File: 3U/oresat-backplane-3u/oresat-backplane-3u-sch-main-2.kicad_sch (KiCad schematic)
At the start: 12 parts

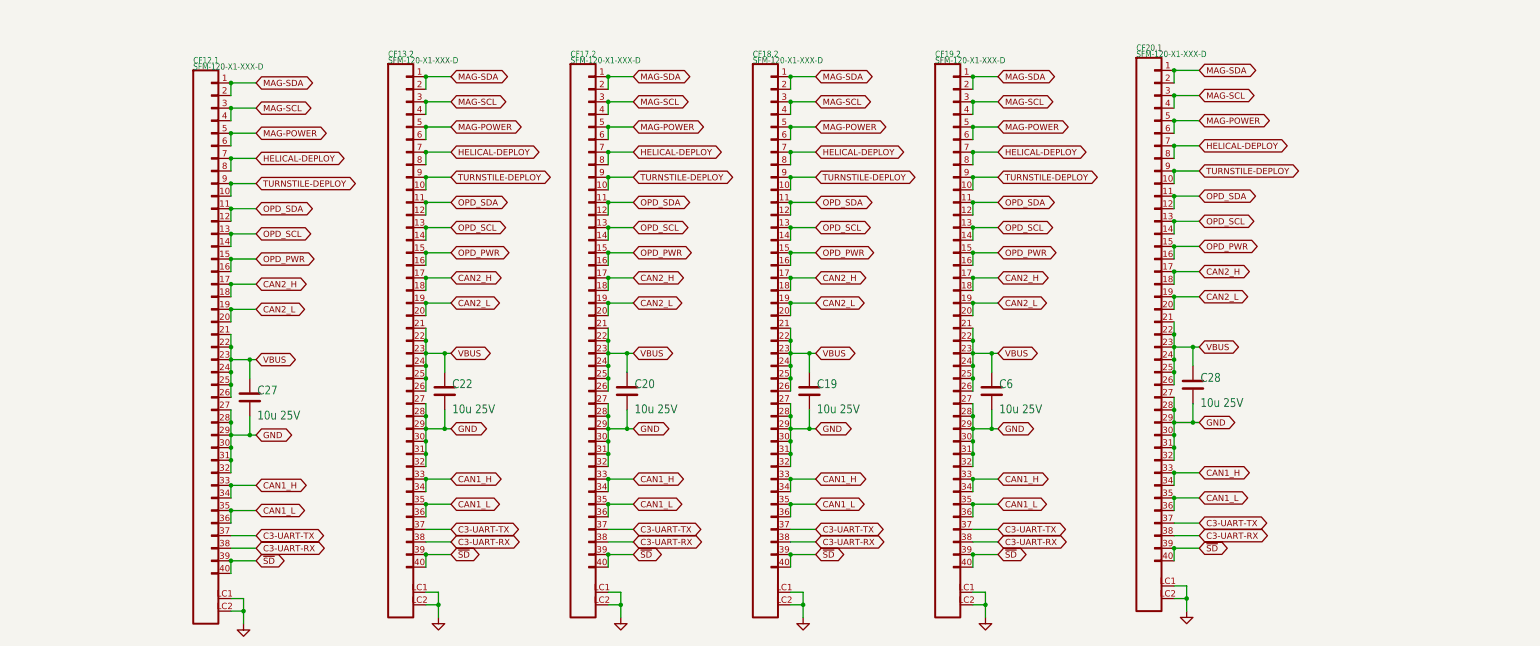
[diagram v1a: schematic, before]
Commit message: Added more Auxiliary connectors
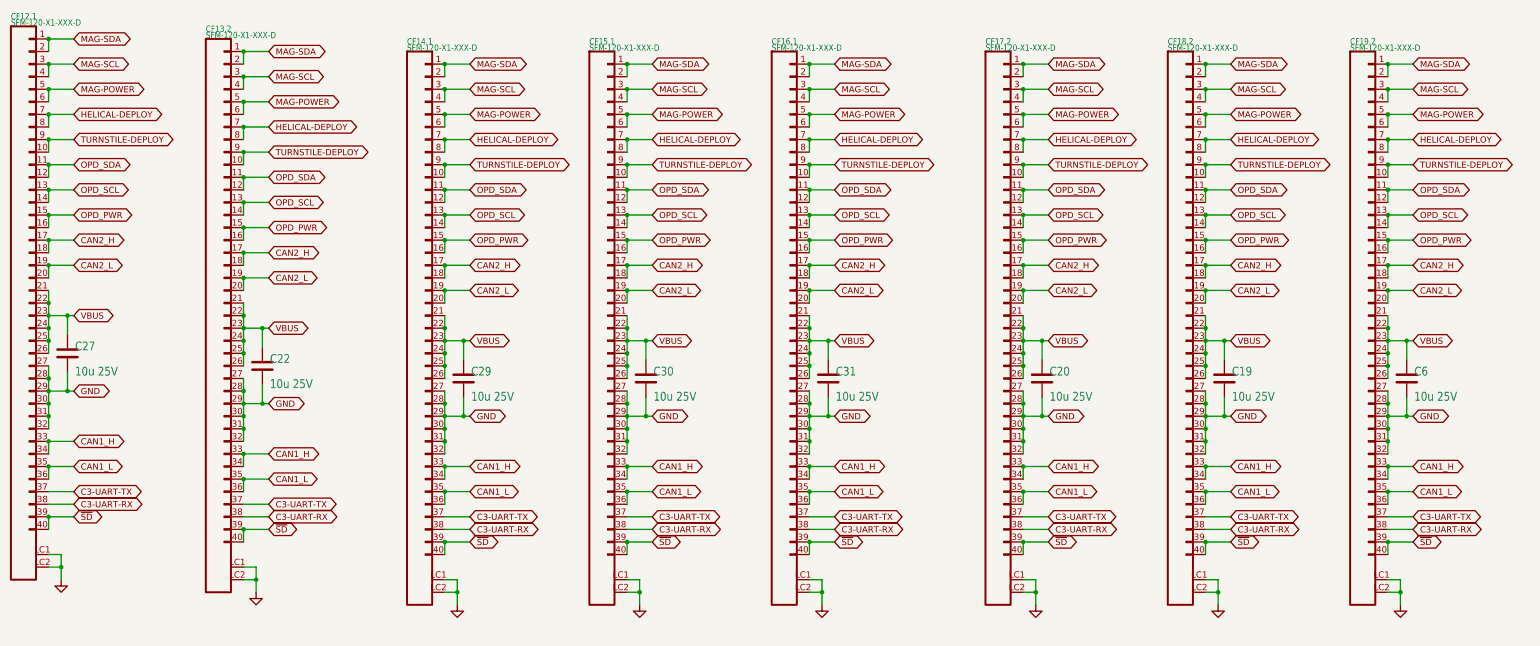
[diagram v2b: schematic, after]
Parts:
- removed C28: 10u 25V, Capacitor_SMD:C_1206_3216Metric, symbol Device:C
- removed CF20.1: SFM-120-X1-XXX-D, oresat-connectors:J-SAMTEC-SFM-120-X1-XXX-D, symbol oresat-connectors:J-SAMTEC-SFM-120-X1-XXX-D
- added C29, C30, C31: 10u 25V, Capacitor_SMD:C_1206_3216Metric, symbol Device:C
- added CF14.1, CF15.1, CF16.1: SFM-120-X1-XXX-D, oresat-connectors:J-SAMTEC-SFM-120-X1-XXX-D, symbol oresat-connectors:J-SAMTEC-SFM-120-X1-XXX-D
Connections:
- net C3-UART-RX: now also CF14.1.38, CF15.1.38, CF16.1.38
- net C3-UART-TX: now also CF14.1.37, CF15.1.37, CF16.1.37
- net CAN1_H: now also CF14.1.33, CF14.1.34, CF15.1.33, CF15.1.34, CF16.1.33, CF16.1.34
- net CAN1_L: now also CF14.1.35, CF14.1.36, CF15.1.35, CF15.1.36, CF16.1.35, CF16.1.36
- net CAN2_H: now also CF14.1.17, CF14.1.18, CF15.1.17, CF15.1.18, CF16.1.17, CF16.1.18
- net CAN2_L: now also CF14.1.19, CF14.1.20, CF15.1.19, CF15.1.20, CF16.1.19, CF16.1.20
- net GND: now also C29.2, C30.2, C31.2, CF14.1.27, CF14.1.28, CF14.1.29, CF14.1.30, CF14.1.31, CF14.1.32, CF14.1.LC1, CF14.1.LC2, CF15.1.27, CF15.1.28, CF15.1.29, CF15.1.30, CF15.1.31, CF15.1.32, CF15.1.LC1, CF15.1.LC2, CF16.1.27, CF16.1.28, CF16.1.29, CF16.1.30, CF16.1.31, CF16.1.32, CF16.1.LC1, CF16.1.LC2
- net HELICAL-DEPLOY: now also CF14.1.7, CF14.1.8, CF15.1.7, CF15.1.8, CF16.1.7, CF16.1.8
- net MAG-POWER: now also CF14.1.5, CF14.1.6, CF15.1.5, CF15.1.6, CF16.1.5, CF16.1.6
- net MAG-SCL: now also CF14.1.3, CF14.1.4, CF15.1.3, CF15.1.4, CF16.1.3, CF16.1.4
- net MAG-SDA: now also CF14.1.1, CF14.1.2, CF15.1.1, CF15.1.2, CF16.1.1, CF16.1.2
- net OPD_PWR: now also CF14.1.15, CF14.1.16, CF15.1.15, CF15.1.16, CF16.1.15, CF16.1.16
- net OPD_SCL: now also CF14.1.13, CF14.1.14, CF15.1.13, CF15.1.14, CF16.1.13, CF16.1.14
- net OPD_SDA: now also CF14.1.11, CF14.1.12, CF15.1.11, CF15.1.12, CF16.1.11, CF16.1.12
- net TURNSTILE-DEPLOY: now also CF14.1.10, CF14.1.9, CF15.1.10, CF15.1.9, CF16.1.10, CF16.1.9
- net VBUS: now also C29.1, C30.1, C31.1, CF14.1.21, CF14.1.22, CF14.1.23, CF14.1.24, CF14.1.25, CF14.1.26, CF15.1.21, CF15.1.22, CF15.1.23, CF15.1.24, CF15.1.25, CF15.1.26, CF16.1.21, CF16.1.22, CF16.1.23, CF16.1.24, CF16.1.25, CF16.1.26
- net ~{SD}: now also CF14.1.39, CF14.1.40, CF15.1.39, CF15.1.40, CF16.1.39, CF16.1.40
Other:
- moved on the sheet: C19, C20, C22, C27, C6, CF12.1, CF13.2, CF17.2, CF18.2, CF19.2

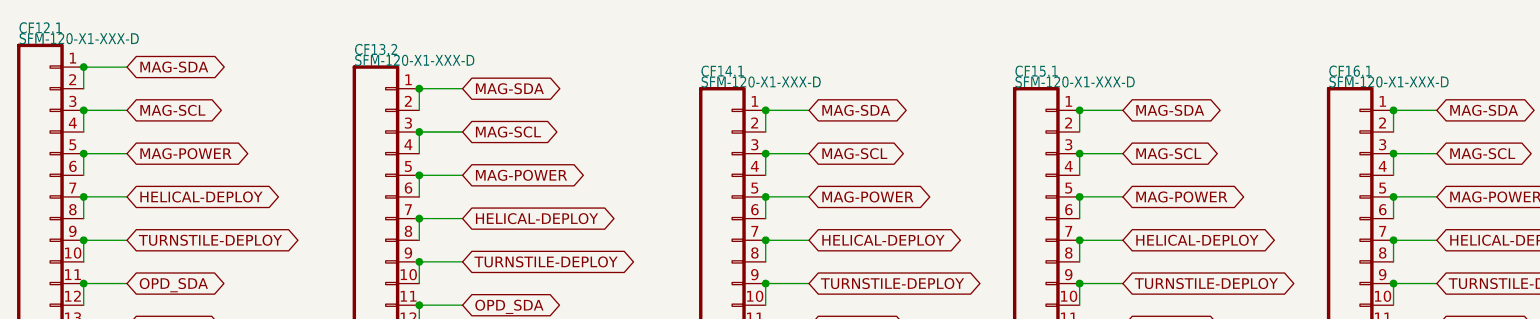
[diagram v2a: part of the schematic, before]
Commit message: Connectors laid out, unrouted
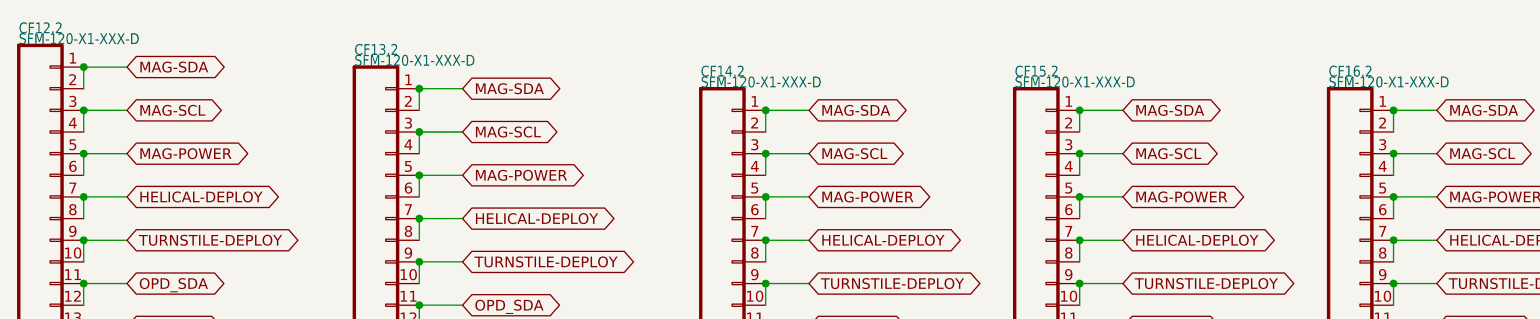
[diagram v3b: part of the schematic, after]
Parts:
- renumbered CF12.1 to CF12.2, CF14.1 to CF14.2, CF15.1 to CF15.2, CF16.1 to CF16.2
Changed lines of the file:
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@@
 		(on_board yes)
 		(dnp no)
-		(property "Reference" "CF12.1"
+		(property "Reference" "CF12.2"
 			(at 76.2 69.85 0)
 			(effects
@@
 			(project "oresat-backplane-3u"
 				(path "/300eeac4-6caf-4310-939c-5dc51539800c/af24dd58-d27a-41e4-b932-04912035cb7a"
-					(reference "CF12.1")
+					(reference "CF12.2")
 					(unit 1)
 				)
@@
 		(on_board yes)
 		(dnp no)
-		(property "Reference" "CF16.1"
+		(property "Reference" "CF16.2"
 			(at 229.87 74.93 0)
 			(effects
@@
 			(project "oresat-backplane-3u"
 				(path "/300eeac4-6caf-4310-939c-5dc51539800c/af24dd58-d27a-41e4-b932-04912035cb7a"
-					(reference "CF16.1")
+					(reference "CF16.2")
 					(unit 1)
 				)
@@
 		(on_board yes)
 		(dnp no)
-		(property "Reference" "CF14.1"
+		(property "Reference" "CF14.2"
 			(at 156.21 74.93 0)
 			(effects
@@
 			(project "oresat-backplane-3u"
 				(path "/300eeac4-6caf-4310-939c-5dc51539800c/af24dd58-d27a-41e4-b932-04912035cb7a"
-					(reference "CF14.1")
+					(reference "CF14.2")
 					(unit 1)
 				)
@@
 		(on_board yes)
 		(dnp no)
-		(property "Reference" "CF15.1"
+		(property "Reference" "CF15.2"
 			(at 193.04 74.93 0)
 			(effects
@@
 			(project "oresat-backplane-3u"
 				(path "/300eeac4-6caf-4310-939c-5dc51539800c/af24dd58-d27a-41e4-b932-04912035cb7a"
-					(reference "CF15.1")
+					(reference "CF15.2")
 					(unit 1)
 				)

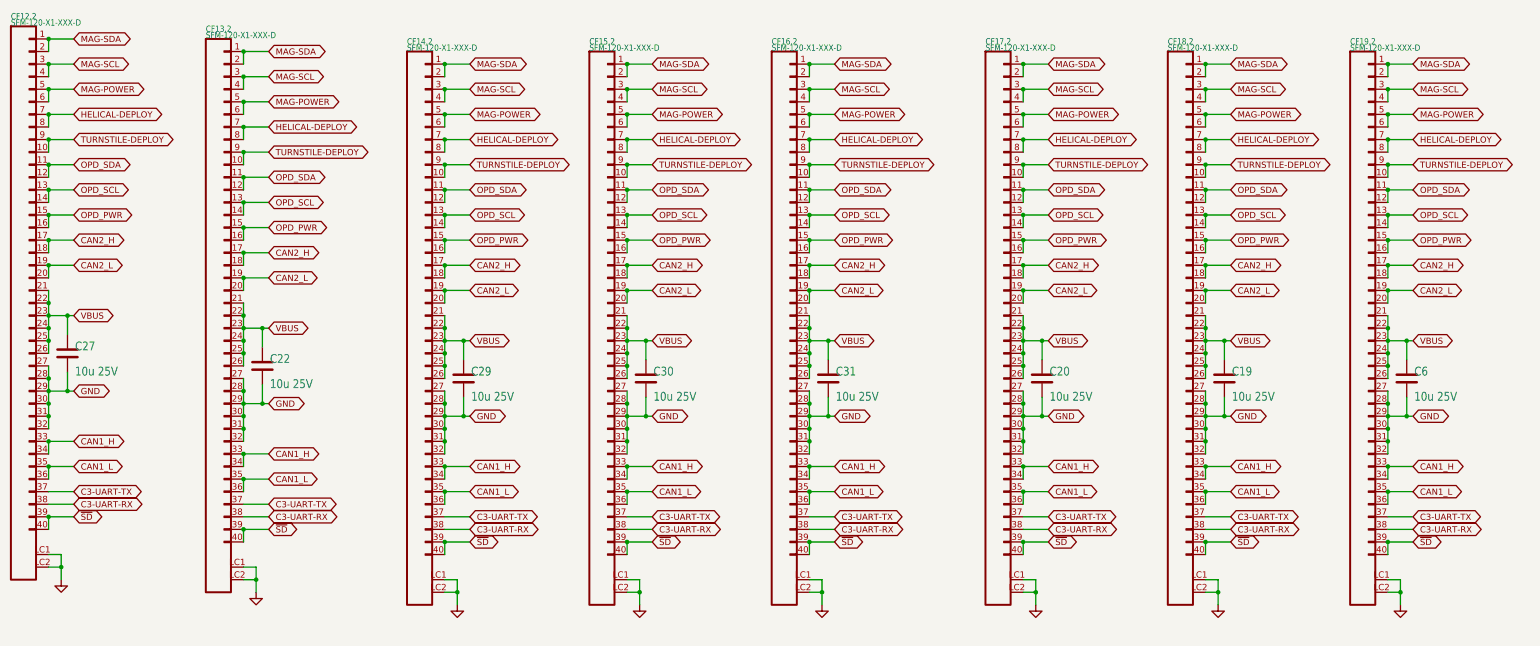
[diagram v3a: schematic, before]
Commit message: Can lines on back - need to move can resistors to front & add b.side solder mask
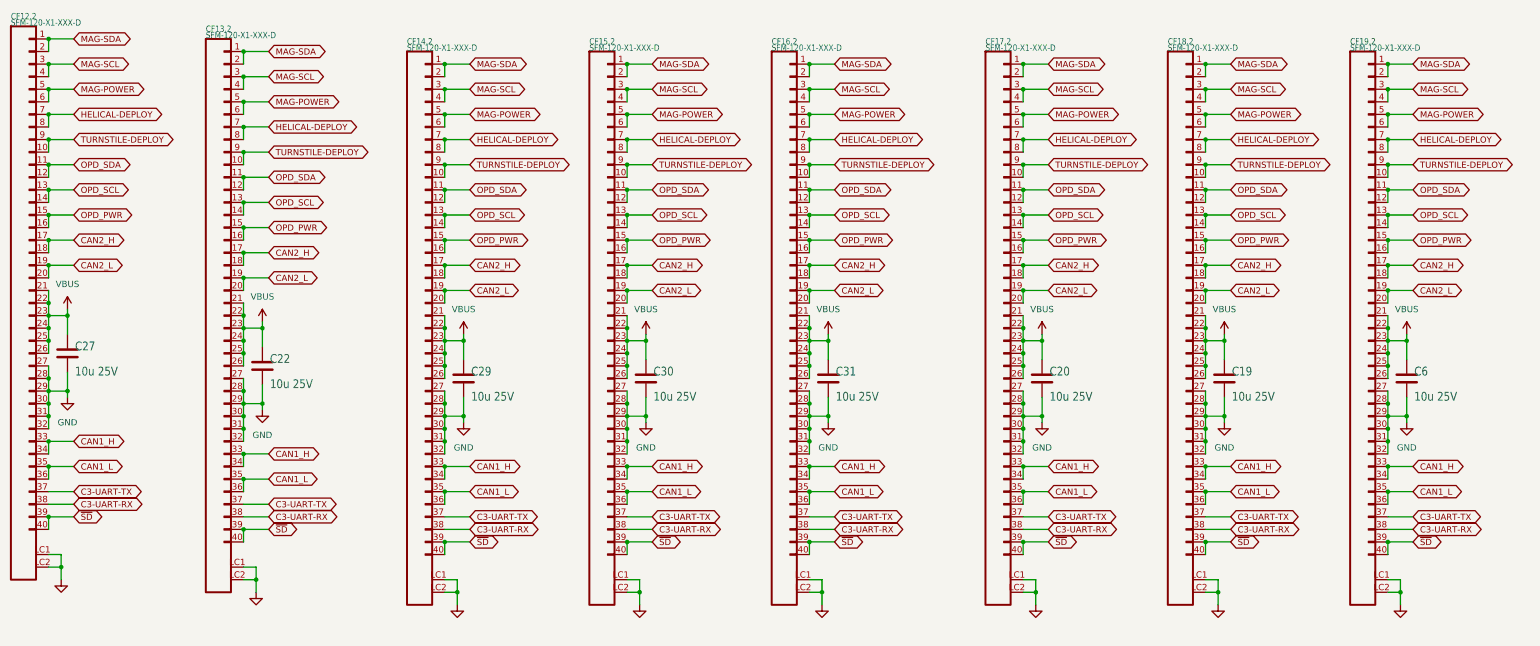
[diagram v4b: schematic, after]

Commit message: Back solder mask added & can resistors moved to F.cu. Final
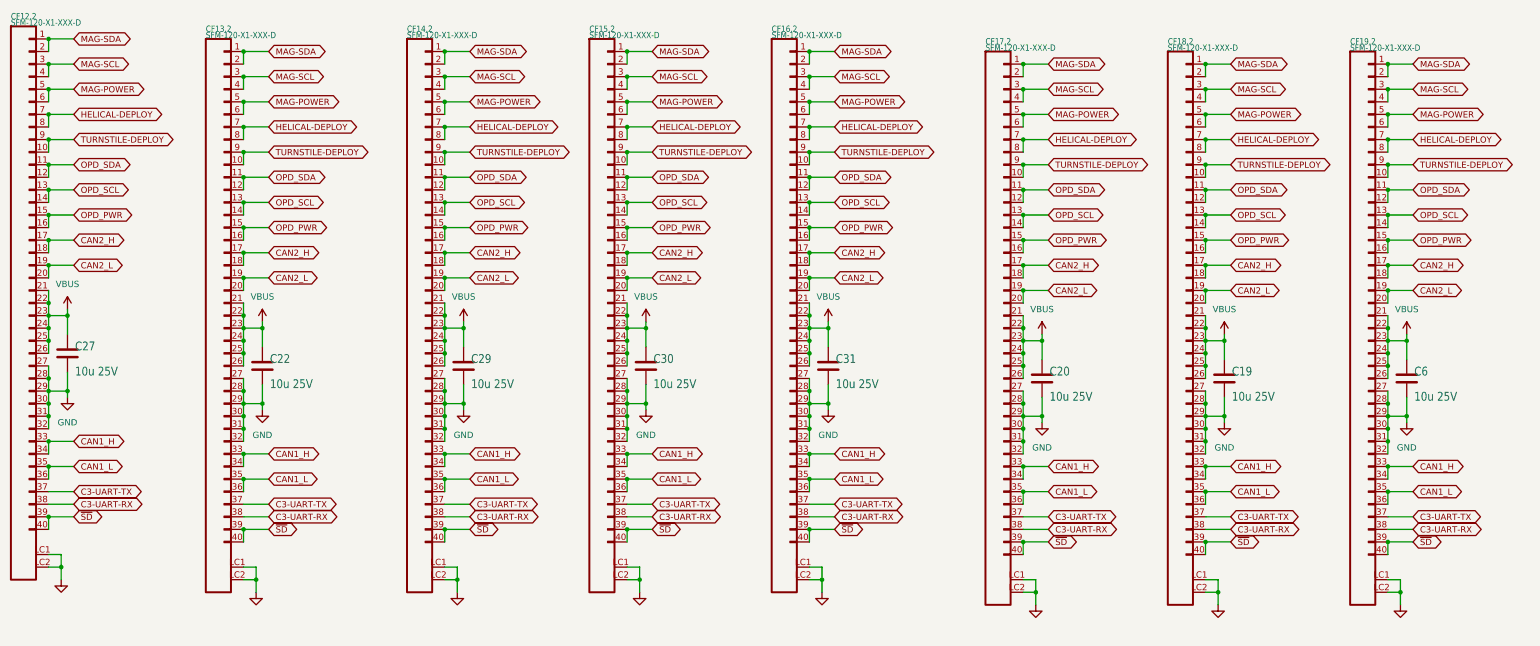
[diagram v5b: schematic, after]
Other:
- moved on the sheet: C29, C30, C31, CF14.2, CF15.2, CF16.2

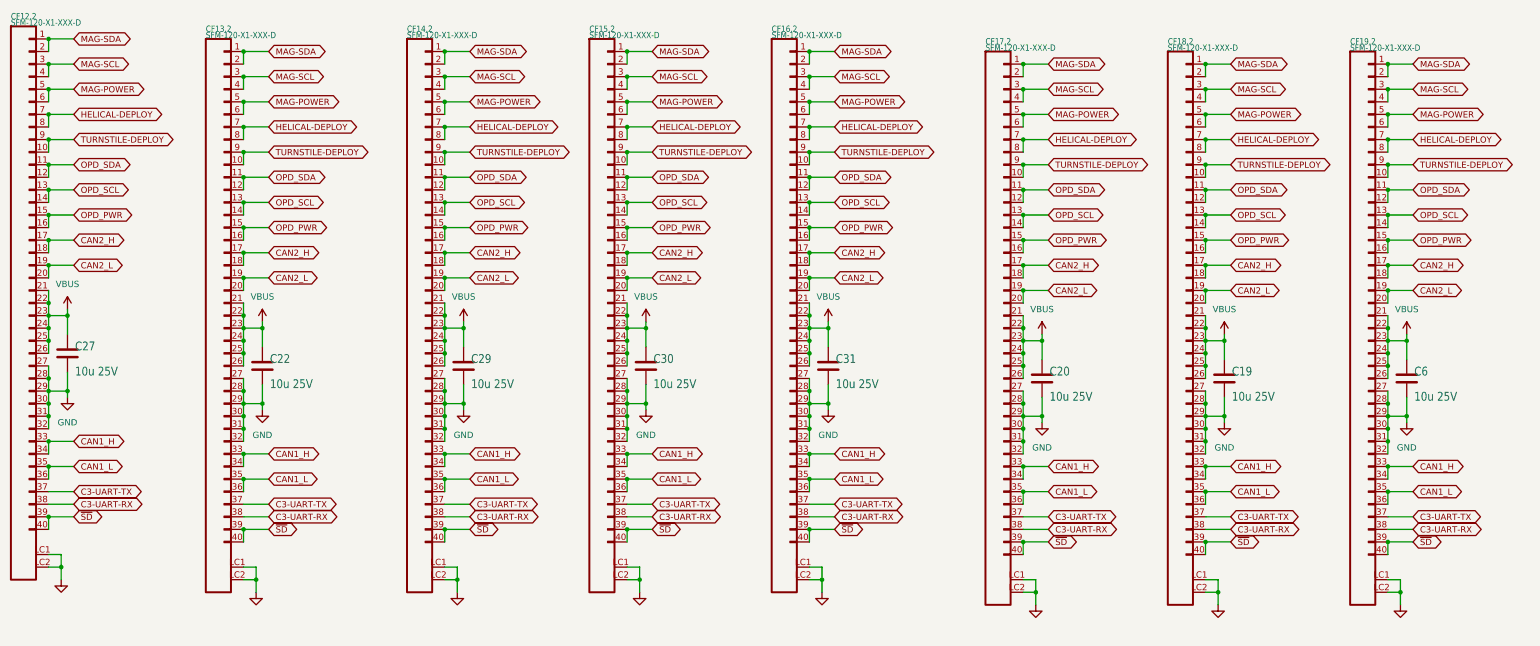
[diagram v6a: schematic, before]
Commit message: updated spare lines on schematic & began tracing
a little more than halfway through
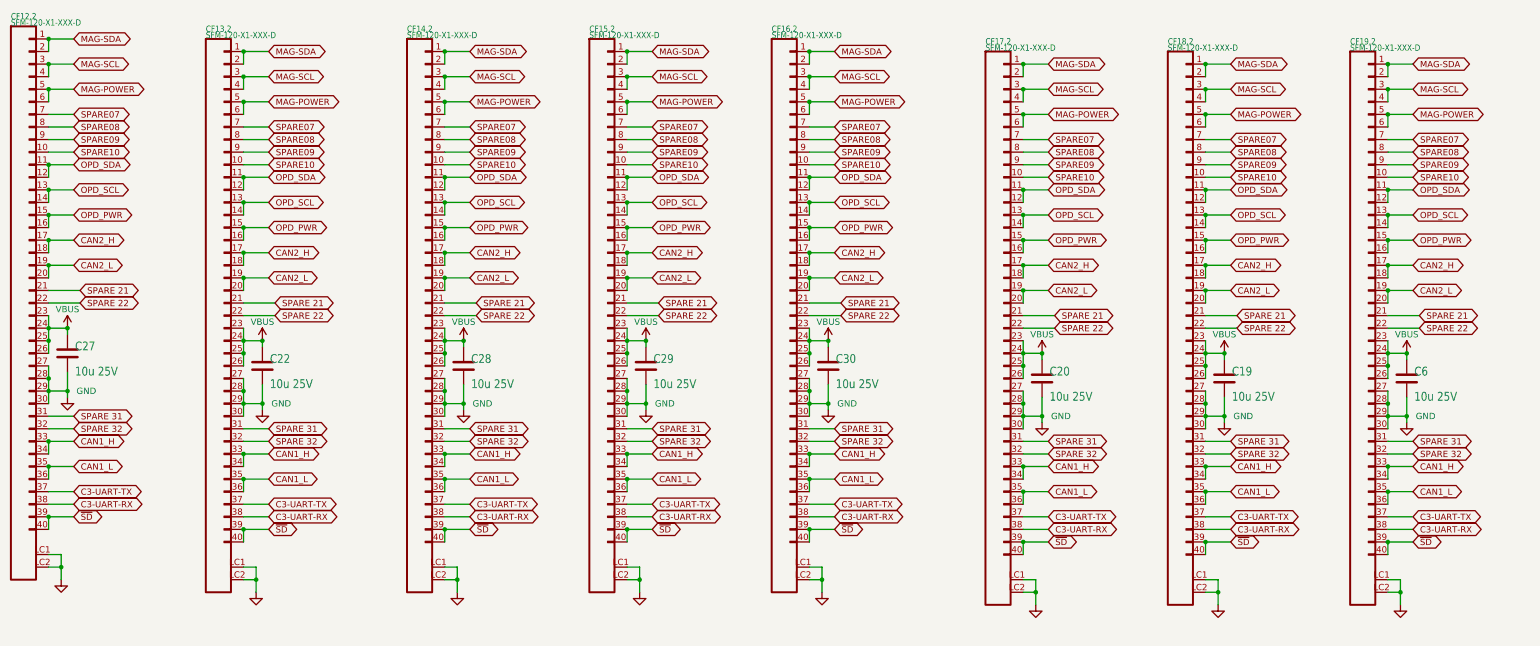
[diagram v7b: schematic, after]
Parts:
- removed C31: 10u 25V, Capacitor_SMD:C_1206_3216Metric, symbol Device:C
- added C28: 10u 25V, Capacitor_SMD:C_1206_3216Metric, symbol Device:C
- C19, C20, C22, C27, C29, C30, C6: DIS (none) -> DigiKey; DPN (none) -> 587-3485-1-ND; MFR (none) -> Taiyo Yuden; MPN (none) -> TMK316AB7106KLHT
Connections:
- net GND: now also C28.2; no longer CF12.2.31, CF12.2.32, CF13.2.31, CF13.2.32, CF14.2.31, CF14.2.32, CF15.2.31, CF15.2.32, CF16.2.31, CF16.2.32, CF17.2.31, CF17.2.32, CF18.2.31, CF18.2.32, CF19.2.31, CF19.2.32
- net VBUS: now also C28.1; no longer CF12.2.21, CF12.2.22, CF13.2.21, CF13.2.22, CF14.2.21, CF14.2.22, CF15.2.21, CF15.2.22, CF16.2.21, CF16.2.22, CF17.2.21, CF17.2.22, CF18.2.21, CF18.2.22, CF19.2.21, CF19.2.22
- net HELICAL-DEPLOY renamed SPARE07
- net SPARE07: no longer CF12.2.8, CF13.2.8, CF14.2.8, CF15.2.8, CF16.2.8, CF17.2.8, CF18.2.8, CF19.2.8
- net TURNSTILE-DEPLOY renamed SPARE09
- net SPARE09: no longer CF12.2.10, CF13.2.10, CF14.2.10, CF15.2.10, CF16.2.10, CF17.2.10, CF18.2.10, CF19.2.10
- new net SPARE 21: CF12.2.21, CF13.2.21, CF14.2.21, CF15.2.21, CF16.2.21, CF17.2.21, CF18.2.21, CF19.2.21
- new net SPARE 22: CF12.2.22, CF13.2.22, CF14.2.22, CF15.2.22, CF16.2.22, CF17.2.22, CF18.2.22, CF19.2.22
- new net SPARE 31: CF12.2.31, CF13.2.31, CF14.2.31, CF15.2.31, CF16.2.31, CF17.2.31, CF18.2.31, CF19.2.31
- new net SPARE 32: CF12.2.32, CF13.2.32, CF14.2.32, CF15.2.32, CF16.2.32, CF17.2.32, CF18.2.32, CF19.2.32
- new net SPARE08: CF12.2.8, CF13.2.8, CF14.2.8, CF15.2.8, CF16.2.8, CF17.2.8, CF18.2.8, CF19.2.8
- new net SPARE10: CF12.2.10, CF13.2.10, CF14.2.10, CF15.2.10, CF16.2.10, CF17.2.10, CF18.2.10, CF19.2.10
